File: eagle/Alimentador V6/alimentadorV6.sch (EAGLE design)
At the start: 21 parts, among them T1 AO3403, T2 AO3403, T3 AO3403, T4 AO3403

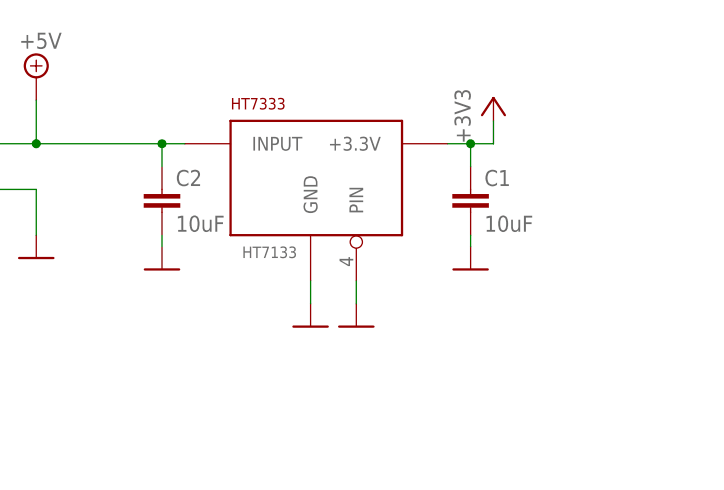
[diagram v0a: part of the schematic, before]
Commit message: Resuelto misterio consumo
Regulador original era una castaña, con el HT7333 consigo 12 uA en la
placa
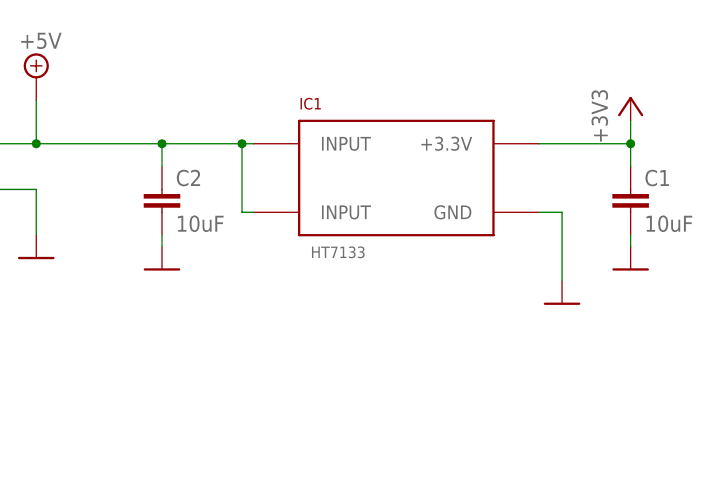
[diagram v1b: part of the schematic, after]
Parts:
- removed HT7333: HT7133, jcf:HT7133
- added IC1: HT7133, jcf:HT7133
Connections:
- net +3V3: now also IC1.+3.3V; no longer HT7333.+3.3V
- net +5V: now also IC1.INPUT@1, IC1.INPUT@2; no longer HT7333.INPUT
- net GND: now also IC1.GND; no longer HT7333.GND, HT7333.PIN
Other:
- moved on the sheet: C1
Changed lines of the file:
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@@
 <setting verticaltext="up"/>
 </settings>
-<grid distance="0.1" unitdist="inch" unit="inch" style="lines" multiple="1" display="no" altdistance="0.01" altunitdist="inch" altunit="inch"/>
+<grid distance="0.05" unitdist="inch" unit="inch" style="lines" multiple="1" display="no" altdistance="0.01" altunitdist="inch" altunit="inch"/>
 <layers>
 <layer number="1" name="Top" color="4" fill="1" visible="no" active="no"/>
@@
 <part name="SUPPLY1" library="supply2" deviceset="+5V" device=""/>
 <part name="SUPPLY3" library="supply2" deviceset="+5V" device=""/>
-<part name="HT7333" library="jcf" deviceset="HT7133" device=""/>
 <part name="+3V1" library="supply1" deviceset="+3V3" device=""/>
 <part name="+3V2" library="supply1" deviceset="+3V3" device=""/>
 <part name="+3V3" library="supply1" deviceset="+3V3" device=""/>
 <part name="GND3" library="supply1" deviceset="GND" device="" value=""/>
-<part name="GND9" library="supply1" deviceset="GND" device="" value=""/>
 <part name="C2" library="rcl" deviceset="C-EU" device="C1206" value="10uF"/>
 <part name="GND5" library="supply1" deviceset="GND" device="" value=""/>
 <part name="C1" library="rcl" deviceset="C-EU" device="C1206" value="10uF"/>
 <part name="GND7" library="supply1" deviceset="GND" device="" value=""/>
+<part name="IC1" library="jcf" deviceset="HT7133" device=""/>
 </parts>
 <sheets>
@@
 <instance part="SUPPLY1" gate="+5V" x="114.3" y="40.3987"/>
 <instance part="SUPPLY3" gate="+5V" x="137.16" y="-95.0087"/>
-<instance part="HT7333" gate="G$1" x="144.78" y="30.48"/>
 <instance part="+3V1" gate="G$1" x="68.58" y="-35.56" rot="R180"/>
 <instance part="+3V2" gate="G$1" x="20.32" y="-77.47" rot="R180"/>
-<instance part="+3V3" gate="G$1" x="165.1" y="38.1"/>
-<instance part="GND3" gate="1" x="144.78" y="12.7"/>
-<instance part="GND9" gate="1" x="149.86" y="12.7"/>
+<instance part="+3V3" gate="G$1" x="180.34" y="38.1"/>
+<instance part="GND3" gate="1" x="172.72" y="15.24"/>
 <instance part="C2" gate="G$1" x="128.27" y="27.94"/>
 <instance part="GND5" gate="1" x="128.27" y="19.05"/>
-<instance part="C1" gate="G$1" x="162.56" y="27.94"/>
-<instance part="GND7" gate="1" x="162.56" y="19.05"/>
+<instance part="C1" gate="G$1" x="180.34" y="27.94"/>
+<instance part="GND7" gate="1" x="180.34" y="19.05"/>
+<instance part="IC1" gate="G$1" x="152.4" y="30.48"/>
 </instances>
 <busses>
@@
 </segment>
 <segment>
-<pinref part="HT7333" gate="G$1" pin="GND"/>
 <pinref part="GND3" gate="1" pin="GND"/>
-<wire x1="144.78" y1="17.78" x2="144.78" y2="15.24" width="0.1524" layer="91"/>
-</segment>
-<segment>
-<pinref part="HT7333" gate="G$1" pin="PIN"/>
-<wire x1="149.86" y1="17.78" x2="149.86" y2="15.24" width="0.1524" layer="91"/>
-<pinref part="GND9" gate="1" pin="GND"/>
+<pinref part="IC1" gate="G$1" pin="GND"/>
+<wire x1="170.18" y1="25.4" x2="172.72" y2="25.4" width="0.1524" layer="91"/>
+<wire x1="172.72" y1="25.4" x2="172.72" y2="17.78" width="0.1524" layer="91"/>
 </segment>
 <segment>
@@
 <pinref part="C1" gate="G$1" pin="2"/>
 <pinref part="GND7" gate="1" pin="GND"/>
-<wire x1="162.56" y1="22.86" x2="162.56" y2="21.59" width="0.1524" layer="91"/>
+<wire x1="180.34" y1="22.86" x2="180.34" y2="21.59" width="0.1524" layer="91"/>
 </segment>
 </net>
@@
 <wire x1="114.3" y1="33.02" x2="114.3" y2="37.8587" width="0.1524" layer="91"/>
 <pinref part="SUPPLY1" gate="+5V" pin="+5V"/>
-<pinref part="HT7333" gate="G$1" pin="INPUT"/>
 <wire x1="114.3" y1="33.02" x2="128.27" y2="33.02" width="0.1524" layer="91"/>
 <junction x="114.3" y="33.02"/>
 <pinref part="C2" gate="G$1" pin="1"/>
-<wire x1="128.27" y1="33.02" x2="130.81" y2="33.02" width="0.1524" layer="91"/>
+<wire x1="128.27" y1="33.02" x2="137.16" y2="33.02" width="0.1524" layer="91"/>
+<wire x1="137.16" y1="33.02" x2="138.43" y2="33.02" width="0.1524" layer="91"/>
 <wire x1="128.27" y1="33.02" x2="128.27" y2="30.48" width="0.1524" layer="91"/>
 <junction x="128.27" y="33.02"/>
+<pinref part="IC1" gate="G$1" pin="INPUT@1"/>
+<wire x1="137.16" y1="33.02" x2="137.16" y2="25.4" width="0.1524" layer="91"/>
+<pinref part="IC1" gate="G$1" pin="INPUT@2"/>
+<wire x1="137.16" y1="25.4" x2="138.43" y2="25.4" width="0.1524" layer="91"/>
+<junction x="137.16" y="33.02"/>
 </segment>
 <segment>
@@
 </segment>
 <segment>
-<pinref part="HT7333" gate="G$1" pin="+3.3V"/>
-<wire x1="160.02" y1="33.02" x2="162.56" y2="33.02" width="0.1524" layer="91"/>
-<wire x1="162.56" y1="33.02" x2="165.1" y2="33.02" width="0.1524" layer="91"/>
-<wire x1="165.1" y1="33.02" x2="165.1" y2="35.56" width="0.1524" layer="91"/>
+<wire x1="180.34" y1="30.48" x2="180.34" y2="33.02" width="0.1524" layer="91"/>
 <pinref part="+3V3" gate="G$1" pin="+3V3"/>
 <pinref part="C1" gate="G$1" pin="1"/>
-<wire x1="162.56" y1="33.02" x2="162.56" y2="30.48" width="0.1524" layer="91"/>
-<junction x="162.56" y="33.02"/>
-</segment>
-</net>
+<pinref part="IC1" gate="G$1" pin="+3.3V"/>
+<wire x1="180.34" y1="33.02" x2="180.34" y2="35.56" width="0.1524" layer="91"/>
+<wire x1="170.18" y1="33.02" x2="180.34" y2="33.02" width="0.1524" layer="91"/>
+<junction x="180.34" y="33.02"/>
+</segment>
+</net>
